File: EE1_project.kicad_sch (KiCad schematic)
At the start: 33 parts, among them J1 GUESS RESISTOR 1, J2 GUESS RESISTOR 2, J3 GUESS RESISTOR 3, J4 POWER, Q1 2N7000, Q2 2N7000, SW1 TEST, U1 LM358

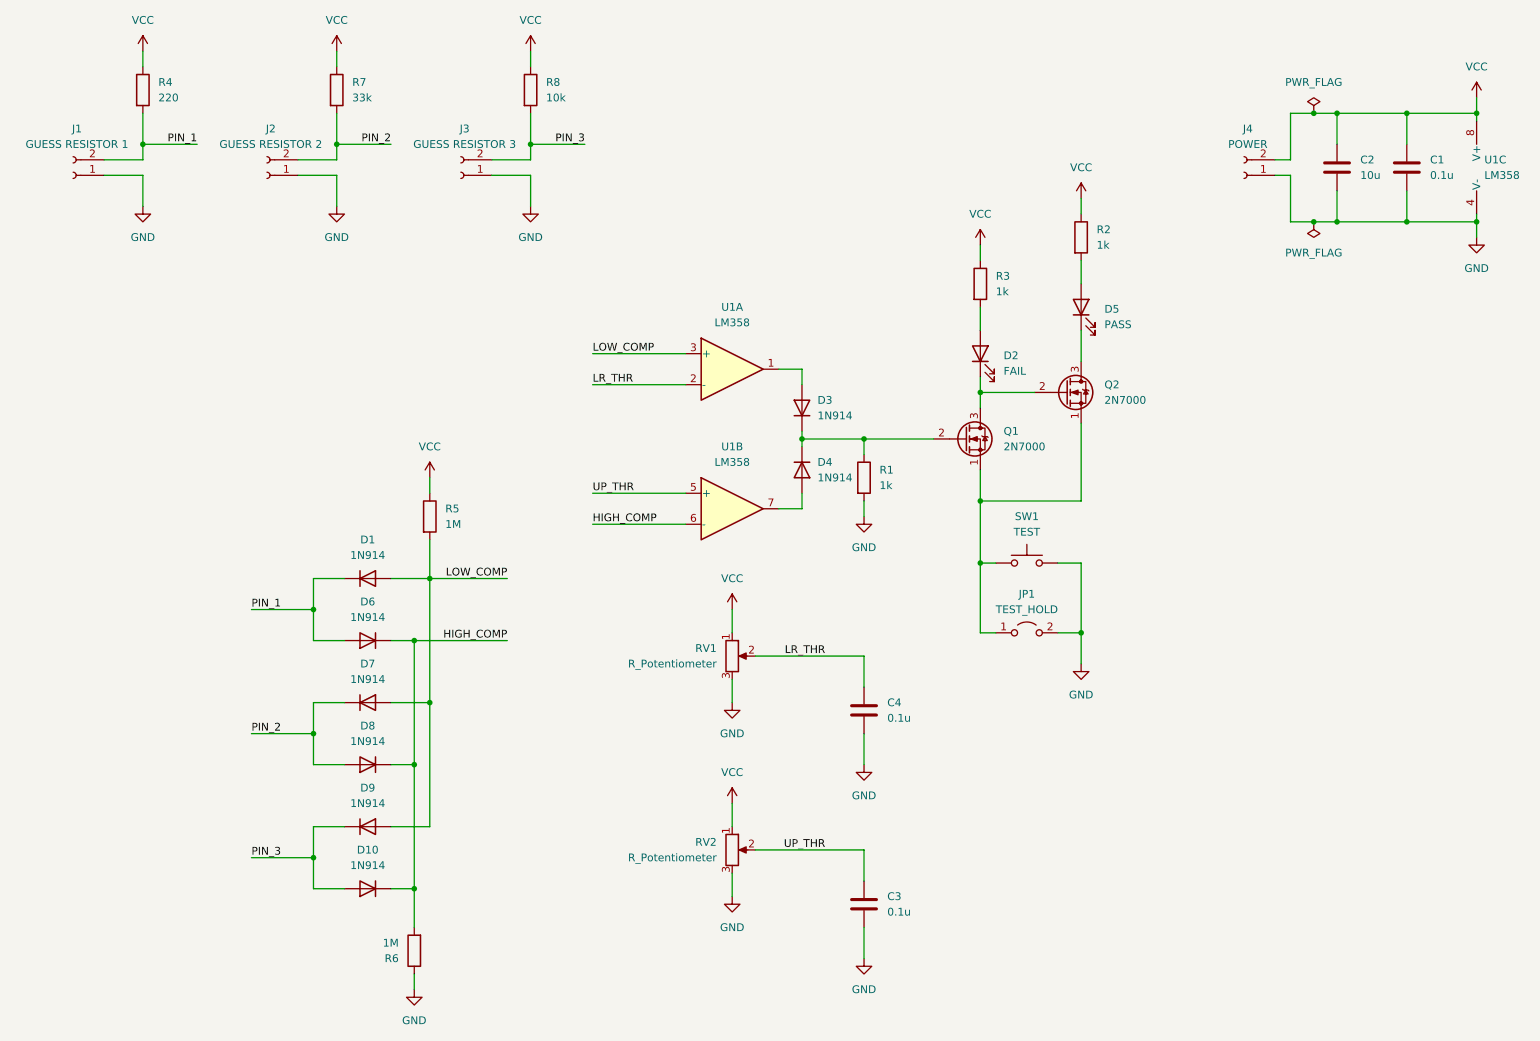
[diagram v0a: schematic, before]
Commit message: flip smd and traces to back
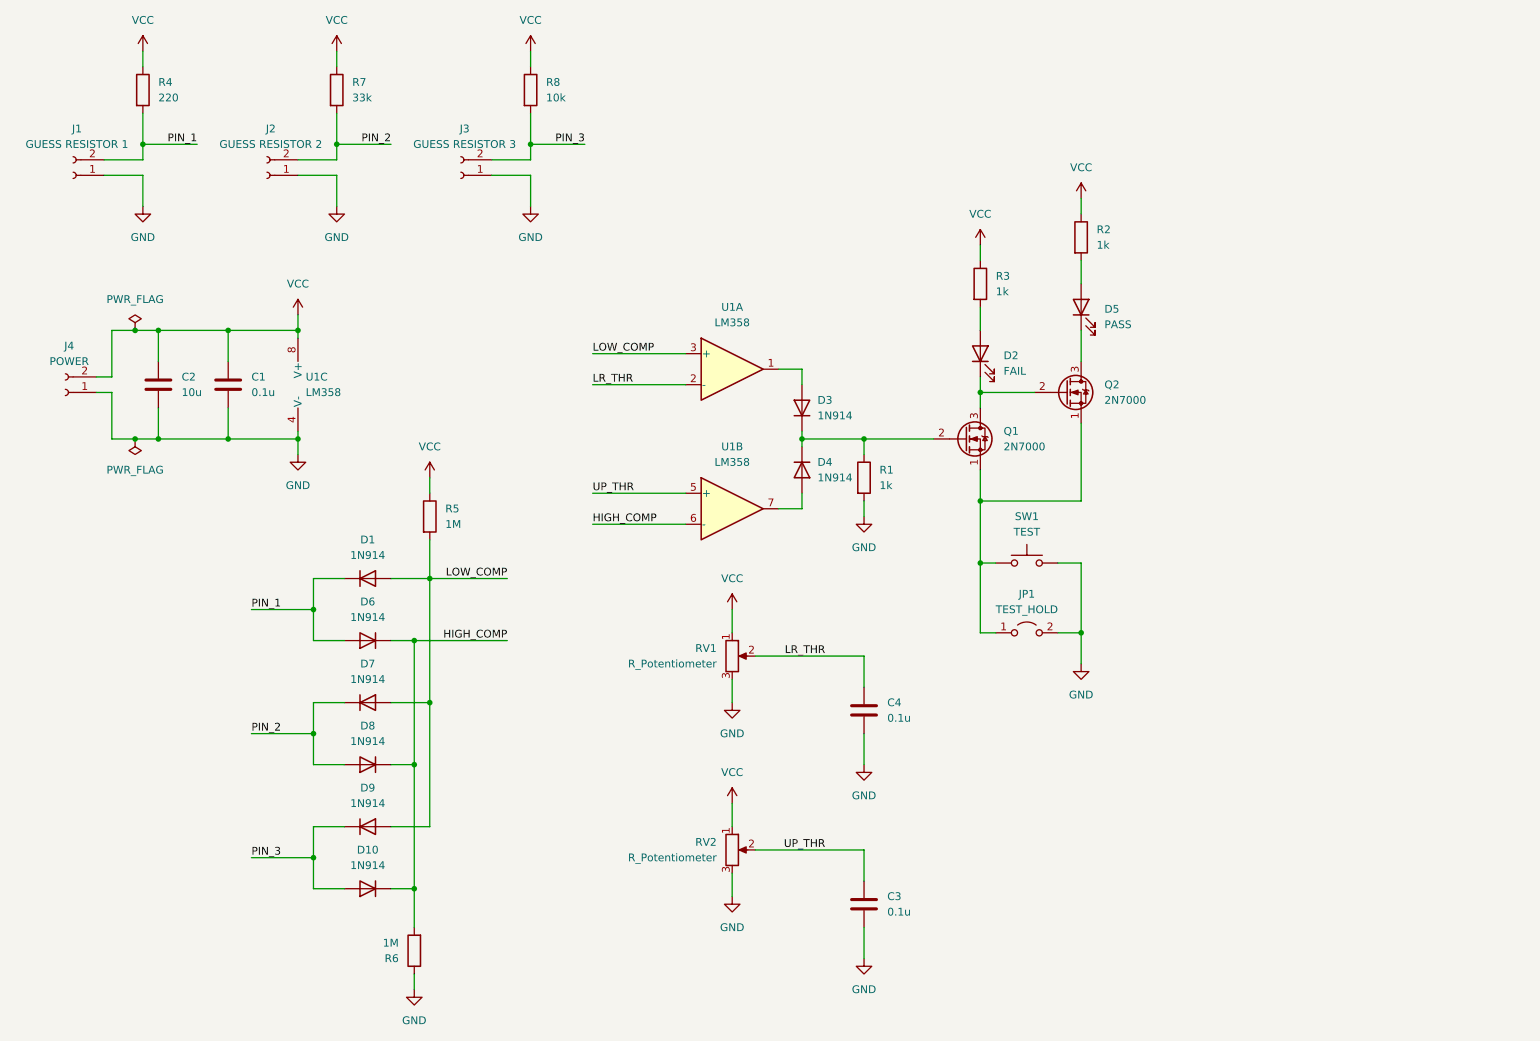
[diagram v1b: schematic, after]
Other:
- moved on the sheet: C1, C2, J4, U1C
